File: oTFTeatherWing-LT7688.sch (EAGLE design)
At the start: 21 parts, among them U1 SPI Flash

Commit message: minor fixes
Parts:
- added R2: 1M, microbuilder:RESISTOR_0603_NOOUT
- C2, C4, C5: value 1uF -> 0.1uF
- R10, R11, R14, R7: value 10K -> 22R
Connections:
- new net LT7688_XI: R2.2, U$1.XI
- new net LT7688_XO: R2.1, U$1.XO
- net QSPI_DATA[0]: now also U1.MISO; no longer U1.MOSI
- net QSPI_DATA[1]: now also U1.MOSI; no longer U1.MISO
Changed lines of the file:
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@@
 <?xml version="1.0" encoding="utf-8"?>
 <!DOCTYPE eagle SYSTEM "eagle.dtd">
-<eagle version="9.6.0">
+<eagle version="9.6.2">
 <drawing>
 <settings>
@@
 <part name="+3V1" library="supply1" library_urn="urn:adsk.eagle:library:371" deviceset="+3V3" device=""/>
 <part name="R6" library="microbuilder" deviceset="RESISTOR" device="_0603_NOOUT" value="10K"/>
-<part name="R7" library="microbuilder" deviceset="RESISTOR" device="_0603_NOOUT" value="10K"/>
-<part name="R10" library="microbuilder" deviceset="RESISTOR" device="_0603_NOOUT" value="10K"/>
-<part name="R11" library="microbuilder" deviceset="RESISTOR" device="_0603_NOOUT" value="10K"/>
-<part name="R14" library="microbuilder" deviceset="RESISTOR" device="_0603_NOOUT" value="10K"/>
+<part name="R7" library="microbuilder" deviceset="RESISTOR" device="_0603_NOOUT" value="22R"/>
+<part name="R10" library="microbuilder" deviceset="RESISTOR" device="_0603_NOOUT" value="22R"/>
+<part name="R11" library="microbuilder" deviceset="RESISTOR" device="_0603_NOOUT" value="22R"/>
+<part name="R14" library="microbuilder" deviceset="RESISTOR" device="_0603_NOOUT" value="22R"/>
 <part name="U$9" library="microbuilder" deviceset="GND" device=""/>
 <part name="U$10" library="microbuilder" deviceset="GND" device=""/>
@@
 <part name="C1" library="microbuilder" deviceset="CAP_CERAMIC" device="0603_NO" value="1uF"/>
 <part name="C3" library="microbuilder" deviceset="CAP_CERAMIC" device="0603_NO" value="1uF"/>
-<part name="C2" library="microbuilder" deviceset="CAP_CERAMIC" device="0603_NO" value="1uF"/>
-<part name="C4" library="microbuilder" deviceset="CAP_CERAMIC" device="0603_NO" value="1uF"/>
-<part name="C5" library="microbuilder" deviceset="CAP_CERAMIC" device="0603_NO" value="1uF"/>
+<part name="C2" library="microbuilder" deviceset="CAP_CERAMIC" device="0603_NO" value="0.1uF"/>
+<part name="C4" library="microbuilder" deviceset="CAP_CERAMIC" device="0603_NO" value="0.1uF"/>
+<part name="C5" library="microbuilder" deviceset="CAP_CERAMIC" device="0603_NO" value="0.1uF"/>
 <part name="+3V2" library="supply1" library_urn="urn:adsk.eagle:library:371" deviceset="+3V3" device=""/>
 <part name="+3V4" library="supply1" library_urn="urn:adsk.eagle:library:371" deviceset="+3V3" device=""/>
@@
 <part name="+3V15" library="supply1" library_urn="urn:adsk.eagle:library:371" deviceset="+3V3" device=""/>
 <part name="+3V16" library="supply1" library_urn="urn:adsk.eagle:library:371" deviceset="+3V3" device=""/>
+<part name="R2" library="microbuilder" deviceset="RESISTOR" device="_0603_NOOUT" value="1M"/>
 </parts>
 <sheets>
@@
 <attribute name="VALUE" x="25.4" y="48.26" size="1.778" layer="96" rot="MR90"/>
 </instance>
+<instance part="R2" gate="G$1" x="162.56" y="203.2" smashed="yes" rot="R90">
+<attribute name="NAME" x="160.02" y="203.2" size="1.27" layer="95" font="vector" rot="R90" align="center"/>
+<attribute name="VALUE" x="162.56" y="203.2" size="1.016" layer="96" font="vector" ratio="15" rot="R90" align="center"/>
+</instance>
 </instances>
 <busses>
@@
 </segment>
 <segment>
-<pinref part="U1" gate="G$1" pin="MOSI"/>
-<wire x1="27.94" y1="40.64" x2="45.72" y2="40.64" width="0.1524" layer="91"/>
-<label x="27.94" y="40.64" size="1.778" layer="95"/>
+<wire x1="27.94" y1="38.1" x2="45.72" y2="38.1" width="0.1524" layer="91"/>
+<label x="27.94" y="38.1" size="1.778" layer="95"/>
+<pinref part="U1" gate="G$1" pin="MISO"/>
 </segment>
 </net>
@@
 </segment>
 <segment>
-<pinref part="U1" gate="G$1" pin="MISO"/>
-<wire x1="45.72" y1="38.1" x2="27.94" y2="38.1" width="0.1524" layer="91"/>
-<label x="27.94" y="38.1" size="1.778" layer="95"/>
+<wire x1="45.72" y1="40.64" x2="27.94" y2="40.64" width="0.1524" layer="91"/>
+<label x="27.94" y="40.64" size="1.778" layer="95"/>
+<pinref part="U1" gate="G$1" pin="MOSI"/>
 </segment>
 </net>
@@
 </segment>
 </net>
+<net name="LT7688_XO" class="0">
+<segment>
+<pinref part="U$1" gate="G$1" pin="XO"/>
+<wire x1="177.8" y1="177.8" x2="147.32" y2="177.8" width="0.1524" layer="91"/>
+<label x="147.32" y="177.8" size="1.778" layer="95"/>
+</segment>
+<segment>
+<wire x1="162.56" y1="198.12" x2="132.08" y2="198.12" width="0.1524" layer="91"/>
+<label x="132.08" y="198.12" size="1.778" layer="95"/>
+<pinref part="R2" gate="G$1" pin="1"/>
+</segment>
+</net>
+<net name="LT7688_XI" class="0">
+<segment>
+<pinref part="U$1" gate="G$1" pin="XI"/>
+<wire x1="198.12" y1="198.12" x2="198.12" y2="220.98" width="0.1524" layer="91"/>
+<label x="198.12" y="203.2" size="1.778" layer="95" rot="R90"/>
+</segment>
+<segment>
+<wire x1="132.08" y1="208.28" x2="162.56" y2="208.28" width="0.1524" layer="91"/>
+<label x="137.16" y="208.28" size="1.778" layer="95"/>
+<pinref part="R2" gate="G$1" pin="2"/>
+</segment>
+</net>

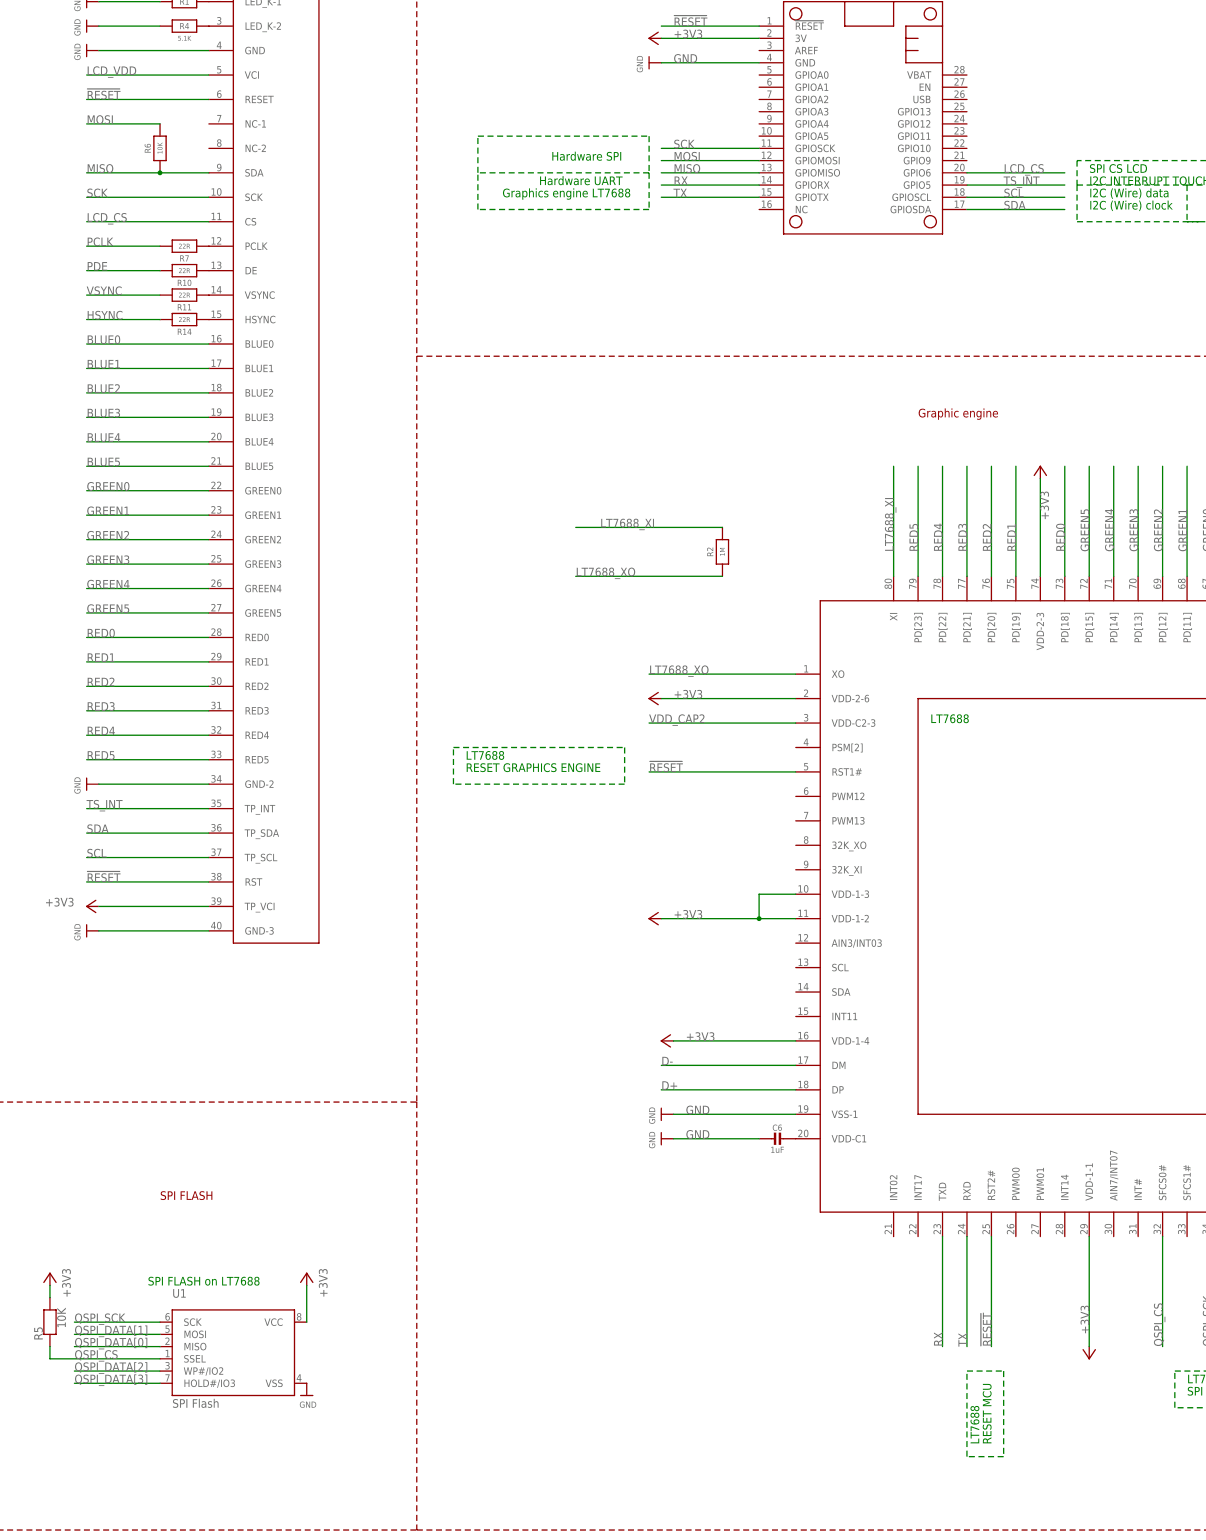
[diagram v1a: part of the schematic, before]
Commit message: changed lcd spi to lt7688
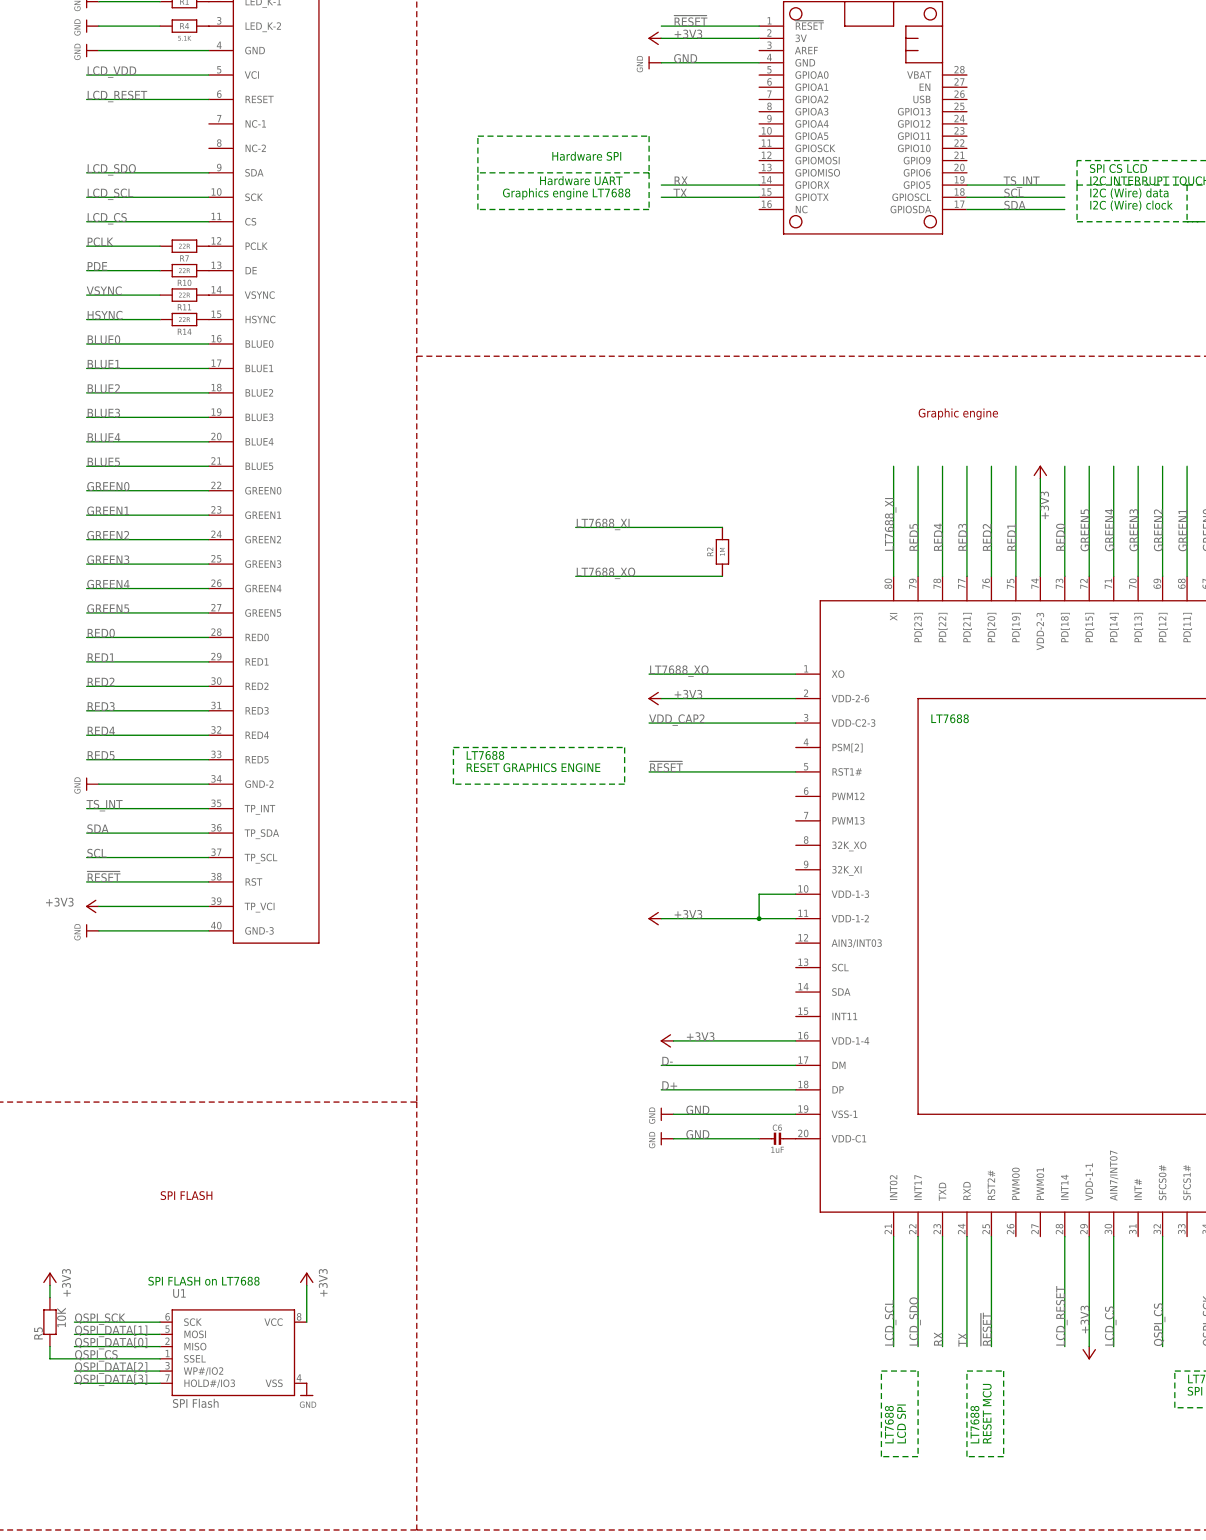
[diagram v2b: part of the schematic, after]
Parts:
- removed R6: 10K, microbuilder:RESISTOR_0603_NOOUT
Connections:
- removed net MISO: MS2.GPIOMISO, R6.1, U$2.SDA
- removed net MOSI: MS2.GPIOMOSI, R6.2
- removed net SCK: MS2.GPIOSCK, U$2.SCK
- new net LCD_RESET: U$1.INT14, U$2.RESET
- new net LCD_SCL: U$1.INT02, U$2.SCK
- new net LCD_SDO: U$1.INT17, U$2.SDA
- net !RESET: no longer U$2.RESET
- net LCD_CS: now also U$1.AIN7/INT07; no longer MS2.GPIO6
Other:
- note added: "LCD SPI"
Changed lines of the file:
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@@
 <?xml version="1.0" encoding="utf-8"?>
 <!DOCTYPE eagle SYSTEM "eagle.dtd">
-<eagle version="9.6.2">
+<eagle version="9.6.0">
 <drawing>
 <settings>
@@
 <part name="U$8" library="microbuilder" deviceset="GND" device=""/>
 <part name="+3V1" library="supply1" library_urn="urn:adsk.eagle:library:371" deviceset="+3V3" device=""/>
-<part name="R6" library="microbuilder" deviceset="RESISTOR" device="_0603_NOOUT" value="10K"/>
 <part name="R7" library="microbuilder" deviceset="RESISTOR" device="_0603_NOOUT" value="22R"/>
 <part name="R10" library="microbuilder" deviceset="RESISTOR" device="_0603_NOOUT" value="22R"/>
@@
 <wire x1="99.06" y1="345.44" x2="0" y2="345.44" width="0.1524" layer="94" style="shortdash"/>
 <wire x1="99.06" y1="345.44" x2="99.06" y2="401.32" width="0.1524" layer="94" style="shortdash"/>
+<text x="200.66" y="17.78" size="1.778" layer="91" rot="R90">LCD SPI</text>
+<text x="198.12" y="17.78" size="1.778" layer="91" rot="R90">LT7688</text>
 </plain>
 <instances>
@@
 </instance>
 <instance part="+3V1" gate="G$1" x="147.32" y="309.88" smashed="yes" rot="MR270"/>
-<instance part="R6" gate="G$1" x="45.72" y="287.02" smashed="yes" rot="R90">
-<attribute name="NAME" x="43.18" y="287.02" size="1.27" layer="95" font="vector" rot="R90" align="center"/>
-<attribute name="VALUE" x="45.72" y="287.02" size="1.016" layer="96" font="vector" ratio="15" rot="R90" align="center"/>
-</instance>
 <instance part="R7" gate="G$1" x="50.8" y="266.7" smashed="yes" rot="R180">
 <attribute name="NAME" x="50.8" y="264.16" size="1.27" layer="95" font="vector" rot="R180" align="center"/>
@@
 </segment>
 <segment>
-<pinref part="U$2" gate="G$1" pin="RESET"/>
-<wire x1="55.88" y1="297.18" x2="30.48" y2="297.18" width="0.1524" layer="91"/>
-<label x="30.48" y="297.18" size="1.778" layer="95"/>
-</segment>
-<segment>
 <pinref part="U$1" gate="G$1" pin="RST2#"/>
 <wire x1="218.44" y1="60.96" x2="218.44" y2="38.1" width="0.1524" layer="91"/>
@@
 </segment>
 </net>
-<net name="LCD_CS" class="0">
-<segment>
-<pinref part="MS2" gate="G$1" pin="GPIO6"/>
-<wire x1="213.36" y1="281.94" x2="233.68" y2="281.94" width="0.1524" layer="91"/>
-<label x="220.98" y="281.94" size="1.778" layer="95"/>
-</segment>
-<segment>
-<pinref part="U$2" gate="G$1" pin="CS"/>
-<wire x1="55.88" y1="271.78" x2="30.48" y2="271.78" width="0.1524" layer="91"/>
-<label x="30.48" y="271.78" size="1.778" layer="95"/>
-</segment>
-</net>
 <net name="SDA" class="0">
 <segment>
@@
 <label x="213.36" y="38.1" size="1.778" layer="95" rot="R90"/>
 <pinref part="U$1" gate="G$1" pin="RXD"/>
-</segment>
-</net>
-<net name="MOSI" class="0">
-<segment>
-<pinref part="MS2" gate="G$1" pin="GPIOMOSI"/>
-<wire x1="170.18" y1="284.48" x2="149.86" y2="284.48" width="0.1524" layer="91"/>
-<label x="152.4" y="284.48" size="1.778" layer="95"/>
-</segment>
-<segment>
-<pinref part="R6" gate="G$1" pin="2"/>
-<wire x1="45.72" y1="292.1" x2="30.48" y2="292.1" width="0.1524" layer="91"/>
-<label x="30.48" y="292.1" size="1.778" layer="95"/>
-</segment>
-</net>
-<net name="MISO" class="0">
-<segment>
-<pinref part="MS2" gate="G$1" pin="GPIOMISO"/>
-<wire x1="170.18" y1="281.94" x2="149.86" y2="281.94" width="0.1524" layer="91"/>
-<label x="152.4" y="281.94" size="1.778" layer="95"/>
-</segment>
-<segment>
-<pinref part="U$2" gate="G$1" pin="SDA"/>
-<pinref part="R6" gate="G$1" pin="1"/>
-<wire x1="55.88" y1="281.94" x2="45.72" y2="281.94" width="0.1524" layer="91"/>
-<wire x1="45.72" y1="281.94" x2="30.48" y2="281.94" width="0.1524" layer="91"/>
-<junction x="45.72" y="281.94"/>
-<label x="30.48" y="281.94" size="1.778" layer="95"/>
-</segment>
-</net>
-<net name="SCK" class="0">
-<segment>
-<pinref part="MS2" gate="G$1" pin="GPIOSCK"/>
-<wire x1="170.18" y1="287.02" x2="149.86" y2="287.02" width="0.1524" layer="91"/>
-<label x="152.4" y="287.02" size="1.778" layer="95"/>
-</segment>
-<segment>
-<pinref part="U$2" gate="G$1" pin="SCK"/>
-<wire x1="55.88" y1="276.86" x2="30.48" y2="276.86" width="0.1524" layer="91"/>
-<label x="30.48" y="276.86" size="1.778" layer="95"/>
 </segment>
 </net>
@@
 <segment>
 <wire x1="132.08" y1="208.28" x2="162.56" y2="208.28" width="0.1524" layer="91"/>
-<label x="137.16" y="208.28" size="1.778" layer="95"/>
+<label x="132.08" y="208.28" size="1.778" layer="95"/>
 <pinref part="R2" gate="G$1" pin="2"/>
 </segment>
 </net>
+<net name="LCD_SCL" class="0">
+<segment>
+<pinref part="U$1" gate="G$1" pin="INT02"/>
+<wire x1="198.12" y1="60.96" x2="198.12" y2="38.1" width="0.1524" layer="91"/>
+<label x="198.12" y="38.1" size="1.778" layer="95" rot="R90"/>
+</segment>
+<segment>
+<wire x1="55.88" y1="276.86" x2="30.48" y2="276.86" width="0.1524" layer="91"/>
+<label x="30.48" y="276.86" size="1.778" layer="95"/>
+<pinref part="U$2" gate="G$1" pin="SCK"/>
+</segment>
+</net>
+<net name="LCD_SDO" class="0">
+<segment>
+<pinref part="U$1" gate="G$1" pin="INT17"/>
+<wire x1="203.2" y1="60.96" x2="203.2" y2="38.1" width="0.1524" layer="91"/>
+<label x="203.2" y="38.1" size="1.778" layer="95" rot="R90"/>
+</segment>
+<segment>
+<wire x1="55.88" y1="281.94" x2="30.48" y2="281.94" width="0.1524" layer="91"/>
+<label x="30.48" y="281.94" size="1.778" layer="95"/>
+<pinref part="U$2" gate="G$1" pin="SDA"/>
+</segment>
+</net>
+<net name="LCD_CS" class="0">
+<segment>
+<pinref part="U$1" gate="G$1" pin="AIN7/INT07"/>
+<wire x1="243.84" y1="60.96" x2="243.84" y2="38.1" width="0.1524" layer="91"/>
+<label x="243.84" y="38.1" size="1.778" layer="95" rot="R90"/>
+</segment>
+<segment>
+<wire x1="55.88" y1="271.78" x2="30.48" y2="271.78" width="0.1524" layer="91"/>
+<label x="30.48" y="271.78" size="1.778" layer="95"/>
+<pinref part="U$2" gate="G$1" pin="CS"/>
+</segment>
+</net>
+<net name="LCD_RESET" class="0">
+<segment>
+<pinref part="U$1" gate="G$1" pin="INT14"/>
+<wire x1="233.68" y1="60.96" x2="233.68" y2="38.1" width="0.1524" layer="91"/>
+<label x="233.68" y="38.1" size="1.778" layer="95" rot="R90"/>
+</segment>
+<segment>
+<wire x1="55.88" y1="297.18" x2="30.48" y2="297.18" width="0.1524" layer="91"/>
+<label x="30.48" y="297.18" size="1.778" layer="95"/>
+<pinref part="U$2" gate="G$1" pin="RESET"/>
+</segment>
+</net>
+<net name="N$1" class="0">
+<segment>
+<wire x1="195.58" y1="33.02" x2="203.2" y2="33.02" width="0.1524" layer="91" style="shortdash"/>
+<wire x1="203.2" y1="33.02" x2="203.2" y2="15.24" width="0.1524" layer="91" style="shortdash"/>
+<wire x1="203.2" y1="15.24" x2="195.58" y2="15.24" width="0.1524" layer="91" style="shortdash"/>
+<wire x1="195.58" y1="15.24" x2="195.58" y2="33.02" width="0.1524" layer="91" style="shortdash"/>
+</segment>
+</net>
